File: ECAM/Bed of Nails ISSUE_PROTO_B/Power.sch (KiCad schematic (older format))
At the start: 5 parts

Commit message: saving out files
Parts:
- gave numbers to parts that had none: 3
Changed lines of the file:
@@
 P 8350 3100
 AR Path="/60B612C1" Ref="TP?"  Part="1"
-AR Path="/607BD428/60B612C1" Ref="TP?"  Part="1"
-F 0 "TP?" H 8222 3105 50  0000 R CNN
+AR Path="/607BD428/60B612C1" Ref="TP35"  Part="1"
+F 0 "TP35" H 8222 3105 50  0000 R CNN
 F 1 "TEST-POINT" H 8350 3450 50  0001 C CNN
 F 2 "TFT_TestPoints:TP_RDPad_D1.0mm" H 8350 3100 50  0001 C CNN
@@
 P 9800 3100
 AR Path="/60B61D5B" Ref="TP?"  Part="1"
-AR Path="/607BD428/60B61D5B" Ref="TP?"  Part="1"
-F 0 "TP?" H 9672 3105 50  0000 R CNN
+AR Path="/607BD428/60B61D5B" Ref="TP36"  Part="1"
+F 0 "TP36" H 9672 3105 50  0000 R CNN
 F 1 "TEST-POINT" H 9800 3450 50  0001 C CNN
 F 2 "TFT_TestPoints:TP_RDPad_D1.0mm" H 9800 3100 50  0001 C CNN
@@
 P 9800 3250
 AR Path="/60B62A98" Ref="TP?"  Part="1"
-AR Path="/607BD428/60B62A98" Ref="TP?"  Part="1"
-F 0 "TP?" H 9672 3255 50  0000 R CNN
+AR Path="/607BD428/60B62A98" Ref="TP37"  Part="1"
+F 0 "TP37" H 9672 3255 50  0000 R CNN
 F 1 "TEST-POINT" H 9800 3600 50  0001 C CNN
 F 2 "TFT_TestPoints:TP_RDPad_D1.0mm" H 9800 3250 50  0001 C CNN

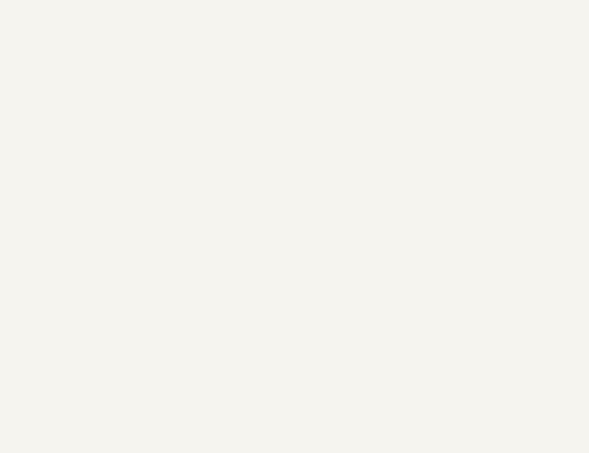
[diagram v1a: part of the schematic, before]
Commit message: updated title blocks and testpoint/connector passthroughs
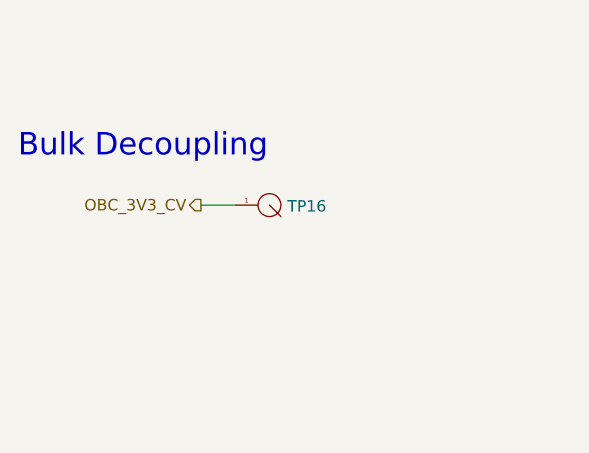
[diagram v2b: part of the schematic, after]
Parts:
- added TP16: TEST-POINT, TFT_TestPoints:TP_RDPad_D1.0mm, symbol TFT_testpoints:TEST-POINT
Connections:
- new net OBC_3V3_CV: TP16.1
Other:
- note added: "Bulk Decoupling"
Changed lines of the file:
@@
 encoding utf-8
 Sheet 4 4
-Title "Singularity OBC - Power Conditioning"
-Date "2021-05-24"
-Rev "PROTO_B_v01"
+Title "Singularity EGSE - Power Conditioning"
+Date "2021-06-05"
+Rev "PROTO_B_v02"
 Comp "The Flame Trench"
 Comment1 "Drawn by:  Ben Cartwright"
@@
 Wire Wire Line
 	9600 3250 9700 3250
+Text Notes 950  2450 0    98   ~ 0
+Bulk Decoupling
+$Comp
+L TFT_testpoints:TEST-POINT TP?
+U 1 1 60D11C02
+P 2000 2650
+AR Path="/60D11C02" Ref="TP?"  Part="1"
+AR Path="/607BD428/60D11C02" Ref="TP16"  Part="1"
+F 0 "TP16" H 1872 2655 50  0000 R CNN
+F 1 "TEST-POINT" H 2000 3000 50  0001 C CNN
+F 2 "TFT_TestPoints:TP_RDPad_D1.0mm" H 2000 2650 50  0001 C CNN
+F 3 "" H 2000 2650 50  0001 C CNN
+	1    2000 2650
+	-1   0    0    1
+$EndComp
+Text HLabel 1750 2650 0    50   Output ~ 0
+OBC_3V3_CV
+Wire Wire Line
+	1750 2650 1900 2650
 $EndSCHEMATC
